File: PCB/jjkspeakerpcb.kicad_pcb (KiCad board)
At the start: 2 copper layers, 125 x 110 mm, 27 parts, among them J1 XIAO_LEFT, J2 XIAO_RIGHT, J3 TFT_8PIN, Q1 2N3904, SW1 UP, SW2 DOWN, SW3 TIME SET, SW4 CLOCK SET, SW5 SNOOZE, SW6 ALARM ON

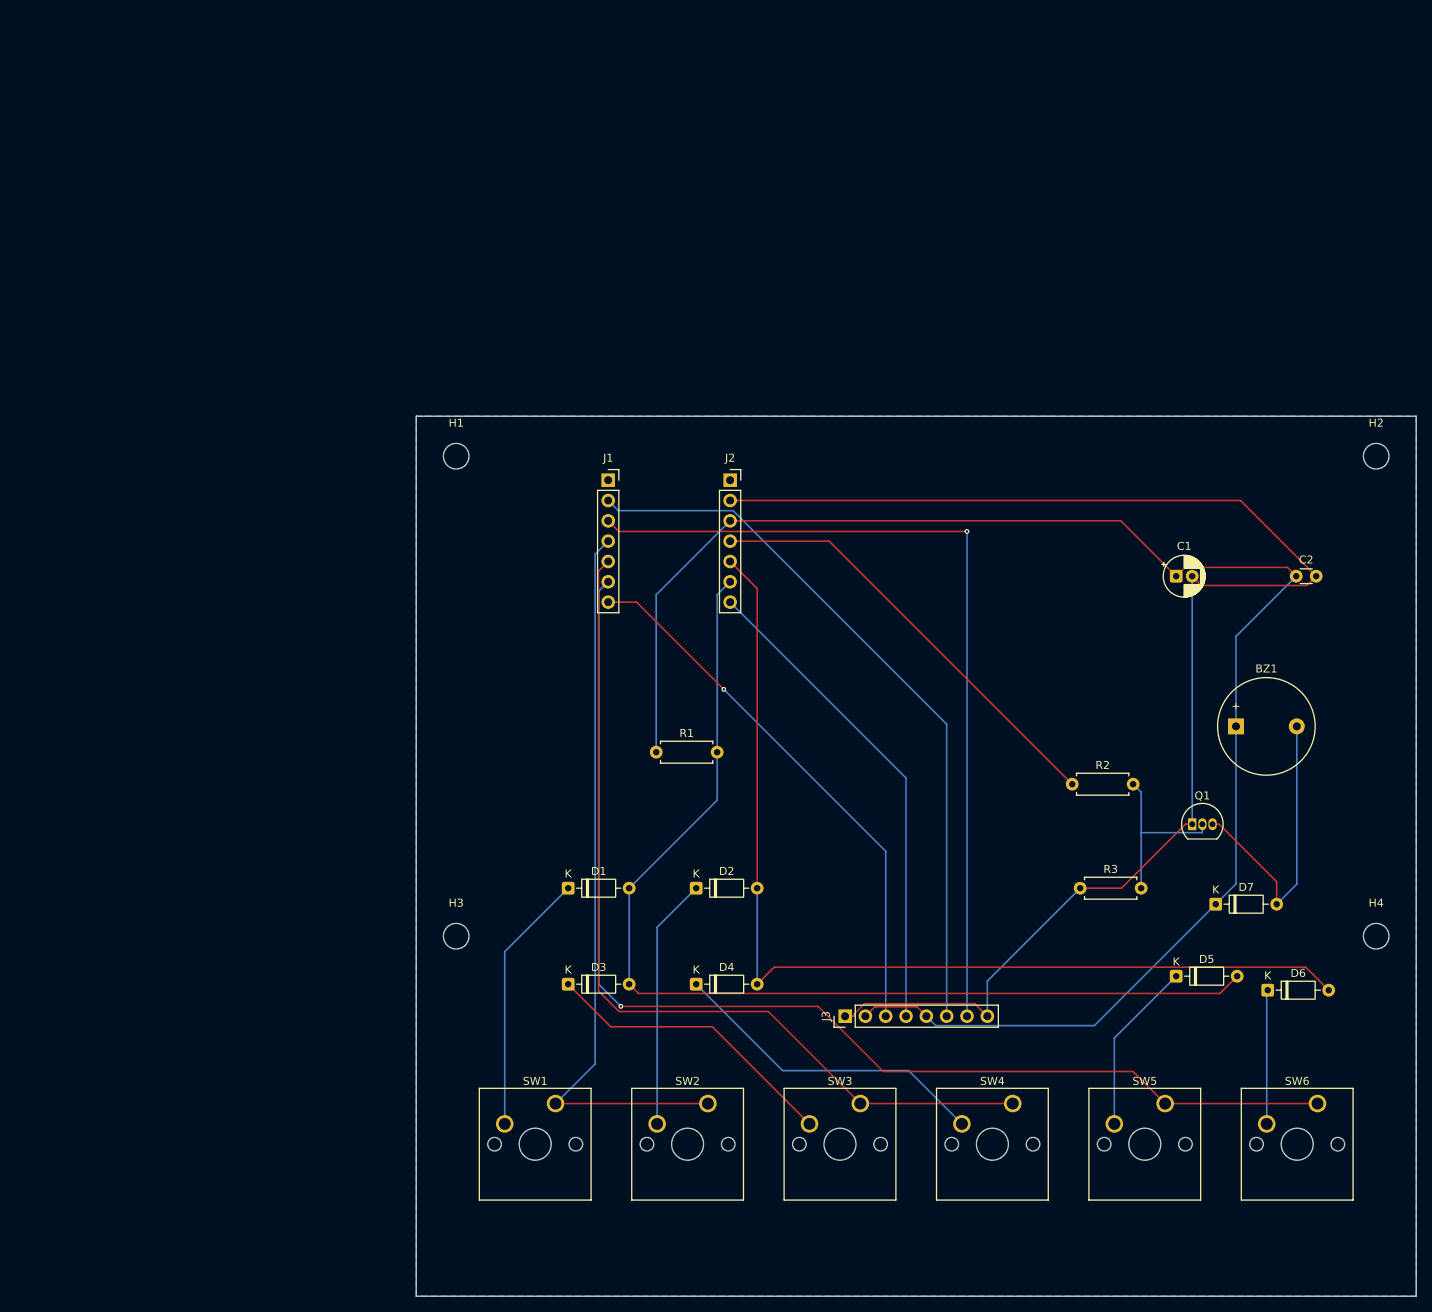
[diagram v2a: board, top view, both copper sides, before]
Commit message: Publish checked 95mm JJK Alarm PCB, full STEP and print parts; retain original 125mm version
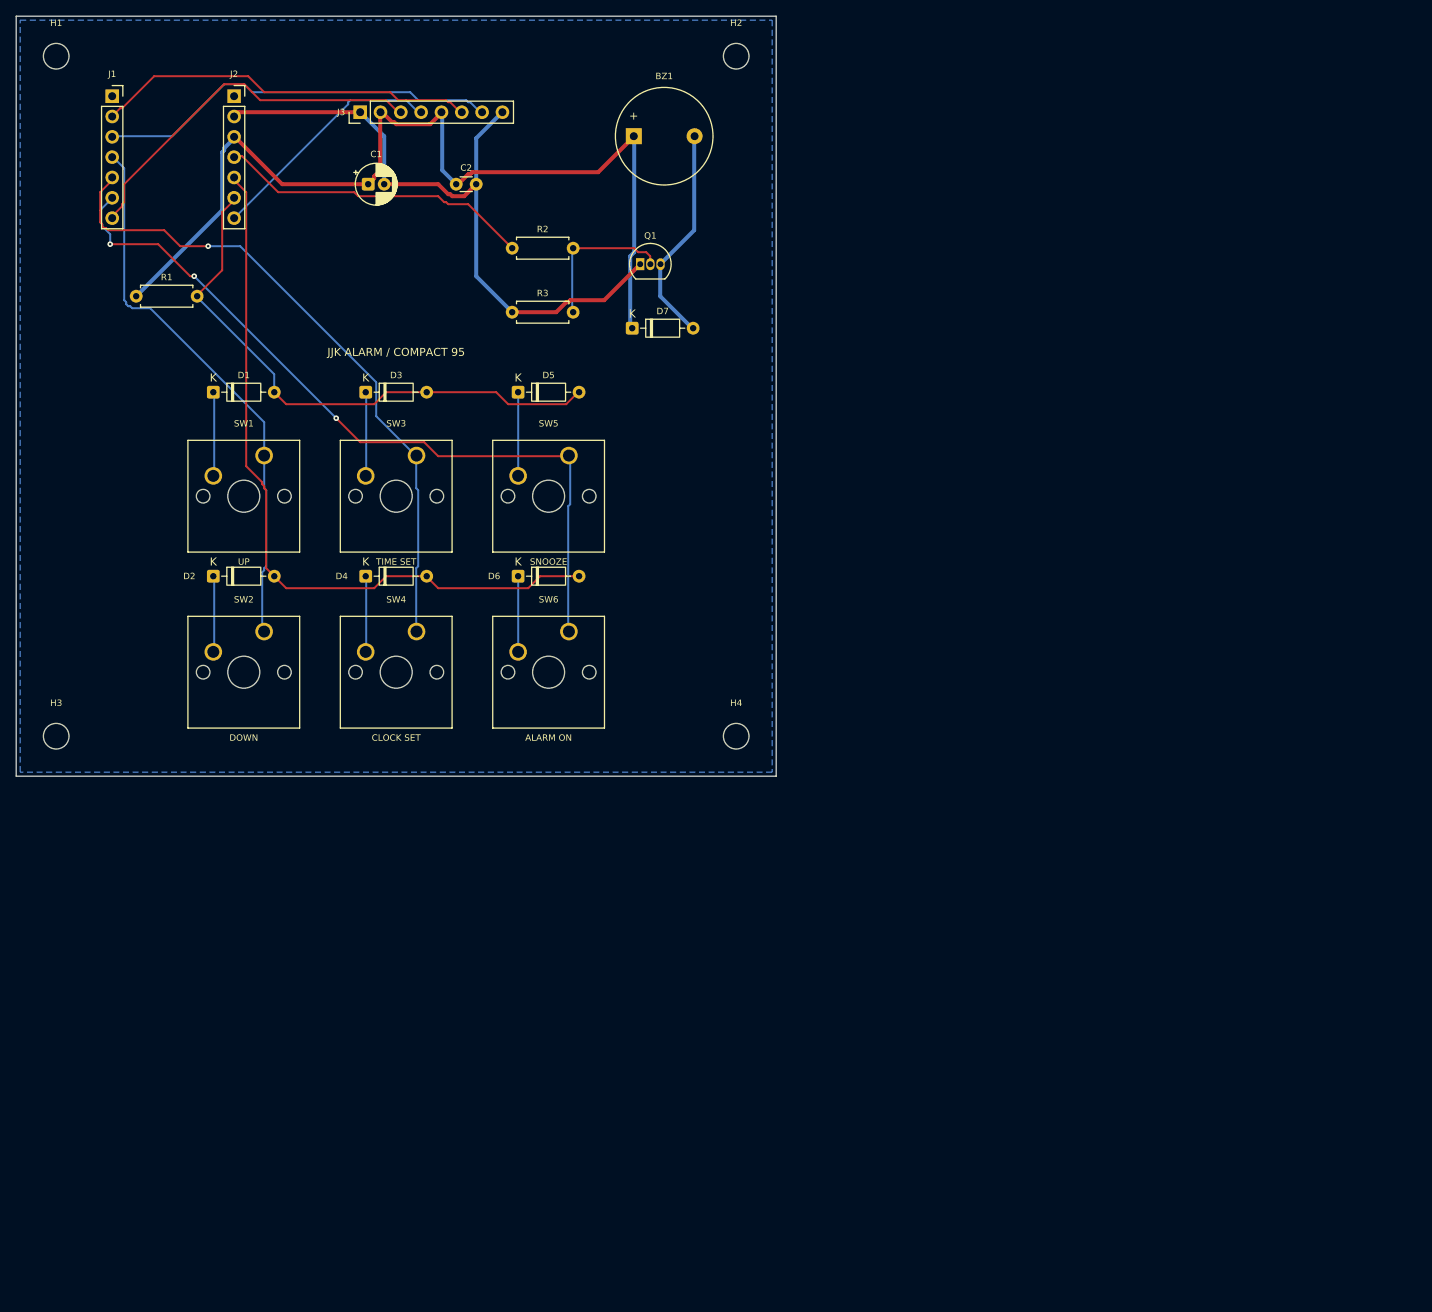
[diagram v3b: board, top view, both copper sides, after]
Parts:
- moved J3 128.2 mm to (43.0, 12.0)
- moved C2 115.9 mm to (55.0, 21.0)
- moved C1 112.3 mm to (44.0, 21.0)
- moved SW6 110.6 mm to (69.1, 76.9)
- moved SW5 110.1 mm to (69.1, 54.9)
- moved D5 110.0 mm to (62.7, 47.0)
- moved D6 107.0 mm to (62.7, 70.0)
- moved BZ1 105.4 mm to (77.2, 15.0)
- moved D7 102.5 mm to (77.0, 39.0)
- moved R3 101.1 mm to (62.0, 37.0)
- moved Q1 98.3 mm to (78.0, 31.0)
- moved SW3 98.2 mm to (50.0, 54.9)
- moved R2 96.9 mm to (62.0, 29.0)
- moved SW4 95.1 mm to (50.0, 76.9)
- moved H2 94.3 mm to (90.0, 5.00)
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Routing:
- net GND: track 182.0 -> 85.7 mm
- net +3V3: track 204.0 -> 122.1 mm
- net /LEFT: track 132.9 -> 71.2 mm
- net /CS: track 106.0 -> 50.5 mm, vias 1 -> 0
- net /BOT: track 146.8 -> 97.7 mm, vias 1 -> 3
- net /DC: track 90.4 -> 47.7 mm
- net /RIGHT: track 127.8 -> 92.6 mm
- net Net-(D4-K): track 40.4 -> 9.63 mm
- net /DISP_MOSI: track 60.9 -> 30.3 mm
- net /MID: track 111.8 -> 82.9 mm, vias 0 -> 1
- net Net-(D3-K): track 37.4 -> 10.6 mm
- net /TOP: track 92.1 -> 69.6 mm
- net /DISP_SCK: track 68.2 -> 46.1 mm, vias 1 -> 0
- net Net-(D1-K): track 32.7 -> 10.7 mm
- net Net-(D2-K): track 31.5 -> 9.73 mm
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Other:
- board size 125 x 110 mm -> 95 x 95 mm
- board text added: "ALARM ON"
- board text added: "CLOCK SET"
- board text added: "DOWN"
- board text added: "JJK ALARM / COMPACT 95"
- board text added: "SNOOZE"
- board text added: "TIME SET"
- board text added: "UP"
